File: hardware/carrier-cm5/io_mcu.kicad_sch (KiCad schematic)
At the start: 33 parts, among them J22 J-LIDAR, J30 TC2050, J31 J-ELRS, J32 U.FL 868 MHz, Q30 MMBT3904, U30 STM32C092KCT6, U31 LR1262

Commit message: cm5 carrier: lora on an rfm95w
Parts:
- removed U31: LR1262, carrier-cm5:LR1262_Elecrow, symbol carrier-cm5-extra:LR1262
- added U31: RFM95W-868S2, RF_Module:HOPERF_RFM9XW_SMD, symbol RF_Module:RFM95W-868S2
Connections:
- net LORA_BUSY is gone; now on net LORA_DIO1: U30.20 (PC6)
- net +3V3: now also U31.13 (3.3V)
- net GND: now also U31.1 (GND), U31.10 (GND), U31.8 (GND)
- net LORA_ANT: now also U31.9 (ANT)
- net LORA_DIO1: now also U31.15 (DIO1); no longer U30.22 (PA11_[PA9])
- net LORA_MISO: now also U31.2 (MISO)
- net LORA_MOSI: now also U31.3 (MOSI)
- net LORA_NRST: now also U31.6 (RESET)
- net LORA_NSS: now also U31.5 (NSS)
- net LORA_SCK: now also U31.4 (SCK)
- new net LORA_DIO0: U30.22 (PA11_[PA9]), U31.14 (DIO0)
- no-connect marks 9 -> 13

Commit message: cm5 carrier: a7670e lte sheet
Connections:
- net LTE_EN: now reaches U30.15 (PB0)
- net LTE_STATUS: now reaches U30.17 (PB2)
- no-connect marks 13 -> 11
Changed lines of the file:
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@@
 	(rectangle
 		(start 17.78 17.78)
-		(end 190.5 172.72)
+		(end 190.5 180.34)
 		(stroke
 			(width 0)
@@
 		)
 	)
-	(no_connect
-		(at 93.98 109.22)
-	)
 	(wire
 		(pts
@@
 		(at 111.76 91.44)
 	)
-	(no_connect
-		(at 111.76 93.98)
-	)
 	(wire
 		(pts
@@
 		)
 	)
+	(wire
+		(pts
+			(xy 93.98 109.22) (xy 93.98 111.76)
+		)
+		(stroke
+			(width 0)
+			(type default)
+		)
+	)
+	(label "LTE_EN"
+		(at 93.98 111.76 270)
+		(fields_autoplaced yes)
+		(effects
+			(font
+				(size 1.27 1.27)
+			)
+			(justify right bottom)
+		)
+	)
+	(wire
+		(pts
+			(xy 111.76 93.98) (xy 114.3 93.98)
+		)
+		(stroke
+			(width 0)
+			(type default)
+		)
+	)
+	(label "LTE_STATUS"
+		(at 114.3 93.98 0)
+		(fields_autoplaced yes)
+		(effects
+			(font
+				(size 1.27 1.27)
+			)
+			(justify left bottom)
+		)
+	)
+	(hierarchical_label "LTE_EN"
+		(shape bidirectional)
+		(at 125.73 170.18 180)
+		(fields_autoplaced yes)
+		(effects
+			(font
+				(size 1.27 1.27)
+			)
+			(justify right)
+		)
+	)
+	(wire
+		(pts
+			(xy 125.73 170.18) (xy 135.89 170.18)
+		)
+		(stroke
+			(width 0)
+			(type default)
+		)
+	)
+	(label "LTE_EN"
+		(at 135.89 170.18 0)
+		(fields_autoplaced yes)
+		(effects
+			(font
+				(size 1.27 1.27)
+			)
+			(justify left bottom)
+		)
+	)
+	(hierarchical_label "LTE_STATUS"
+		(shape bidirectional)
+		(at 125.73 173.99 180)
+		(fields_autoplaced yes)
+		(effects
+			(font
+				(size 1.27 1.27)
+			)
+			(justify right)
+		)
+	)
+	(wire
+		(pts
+			(xy 125.73 173.99) (xy 135.89 173.99)
+		)
+		(stroke
+			(width 0)
+			(type default)
+		)
+	)
+	(label "LTE_STATUS"
+		(at 135.89 173.99 0)
+		(fields_autoplaced yes)
+		(effects
+			(font
+				(size 1.27 1.27)
+			)
+			(justify left bottom)
+		)
+	)

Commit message: Updated schematic on CM5 carrier
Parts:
- renumbered BZ30 to BZ601, C80 to C601, C82 to C602, C81 to C603, C83 to C604, C84 to C605, C85 to C606, C86 to C607, C87 to C608, D80 to D601, D81 to D602, J30 to J601, J22 to J602, J31 to J603, J32 to J604, JP30 to JP601, JP31 to JP602, JP32 to JP603, JP33 to JP604, JP34 to JP605, Q30 to Q601, R80 to R601, R83 to R602, R84 to R603, R81 to R604, R82 to R605, R85 to R606, R86 to R607, R87 to R608, R89 to R609, R88 to R610, U30 to U601, U31 to U602
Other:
- company: AAC -> (none)
- moved on the sheet: C604, J602, J603, J604, JP605, R602, R603, R604, R605

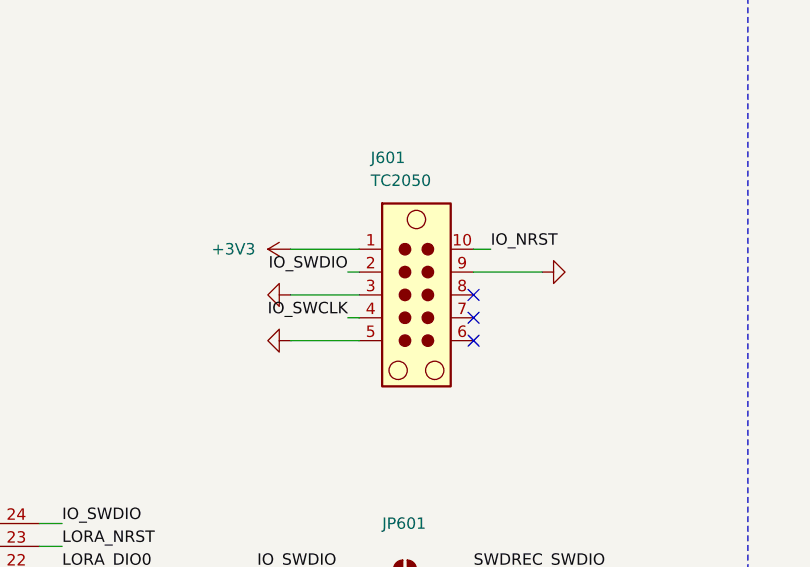
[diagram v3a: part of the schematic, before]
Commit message: carrier: xh can and sysctl connectors, io mcu wiring tidy
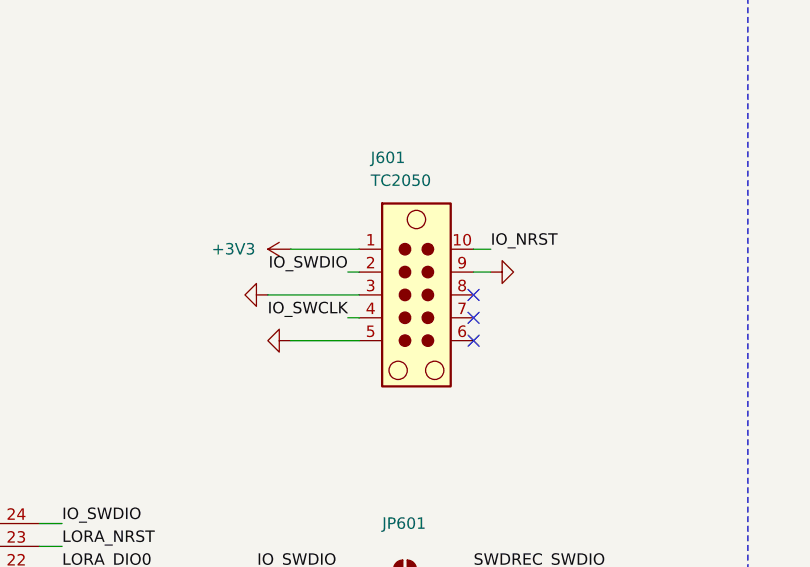
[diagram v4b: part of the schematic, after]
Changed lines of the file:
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@@
 	(wire
 		(pts
-			(xy 160.02 48.26) (xy 167.64 48.26)
+			(xy 160.02 48.26) (xy 161.925 48.26)
 		)
 		(stroke
@@
 	(wire
 		(pts
-			(xy 147.32 50.8) (xy 139.7 50.8)
+			(xy 147.32 50.8) (xy 137.16 50.8)
 		)
 		(stroke
@@
 	(symbol
 		(lib_id "power:GND")
-		(at 139.7 50.8 270)
+		(at 137.16 50.8 270)
 		(unit 1)
 		(body_style 1)
@@
 		(dnp no)
 		(property "Reference" "#PWR0610"
-			(at 139.7 57.15 0)
+			(at 137.16 57.15 0)
 			(hide yes)
 			(show_name no)
@@
 		)
 		(property "Value" "GND"
-			(at 139.7 54.61 0)
+			(at 137.16 54.61 0)
 			(hide yes)
 			(show_name no)
@@
 		)
 		(property "Footprint" ""
-			(at 139.7 50.8 0)
+			(at 137.16 50.8 0)
 			(show_name no)
 			(do_not_autoplace no)
@@
 		)
 		(property "Datasheet" ""
-			(at 139.7 50.8 0)
+			(at 137.16 50.8 0)
 			(show_name no)
 			(do_not_autoplace no)
@@
 		)
 		(property "Description" ""
-			(at 139.7 50.8 0)
+			(at 137.16 50.8 0)
 			(show_name no)
 			(do_not_autoplace no)
@@
 	(symbol
 		(lib_id "power:GND")
-		(at 167.64 48.26 90)
+		(at 161.925 48.26 90)
 		(unit 1)
 		(body_style 1)
@@
 		(dnp no)
 		(property "Reference" "#PWR0612"
-			(at 167.64 54.61 0)
+			(at 161.925 54.61 0)
 			(hide yes)
 			(show_name no)
@@
 		)
 		(property "Value" "GND"
-			(at 167.64 52.07 0)
+			(at 161.925 52.07 0)
 			(hide yes)
 			(show_name no)
@@
 		)
 		(property "Footprint" ""
-			(at 167.64 48.26 0)
+			(at 161.925 48.26 0)
 			(show_name no)
 			(do_not_autoplace no)
@@
 		)
 		(property "Datasheet" ""
-			(at 167.64 48.26 0)
+			(at 161.925 48.26 0)
 			(show_name no)
 			(do_not_autoplace no)
@@
 		)
 		(property "Description" ""
-			(at 167.64 48.26 0)
+			(at 161.925 48.26 0)
 			(show_name no)
 			(do_not_autoplace no)

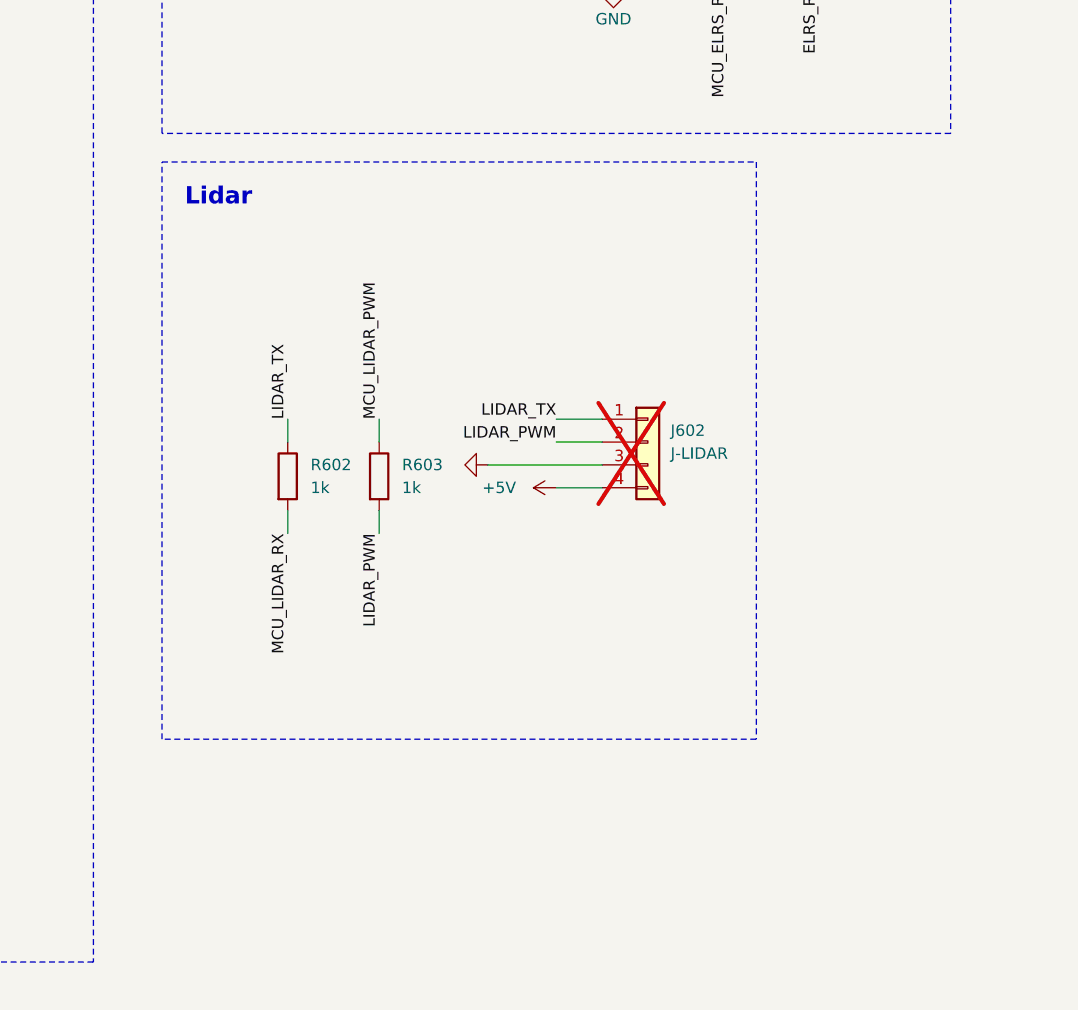
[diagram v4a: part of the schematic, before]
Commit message: add lidar motor fet and xh connectors on carrier
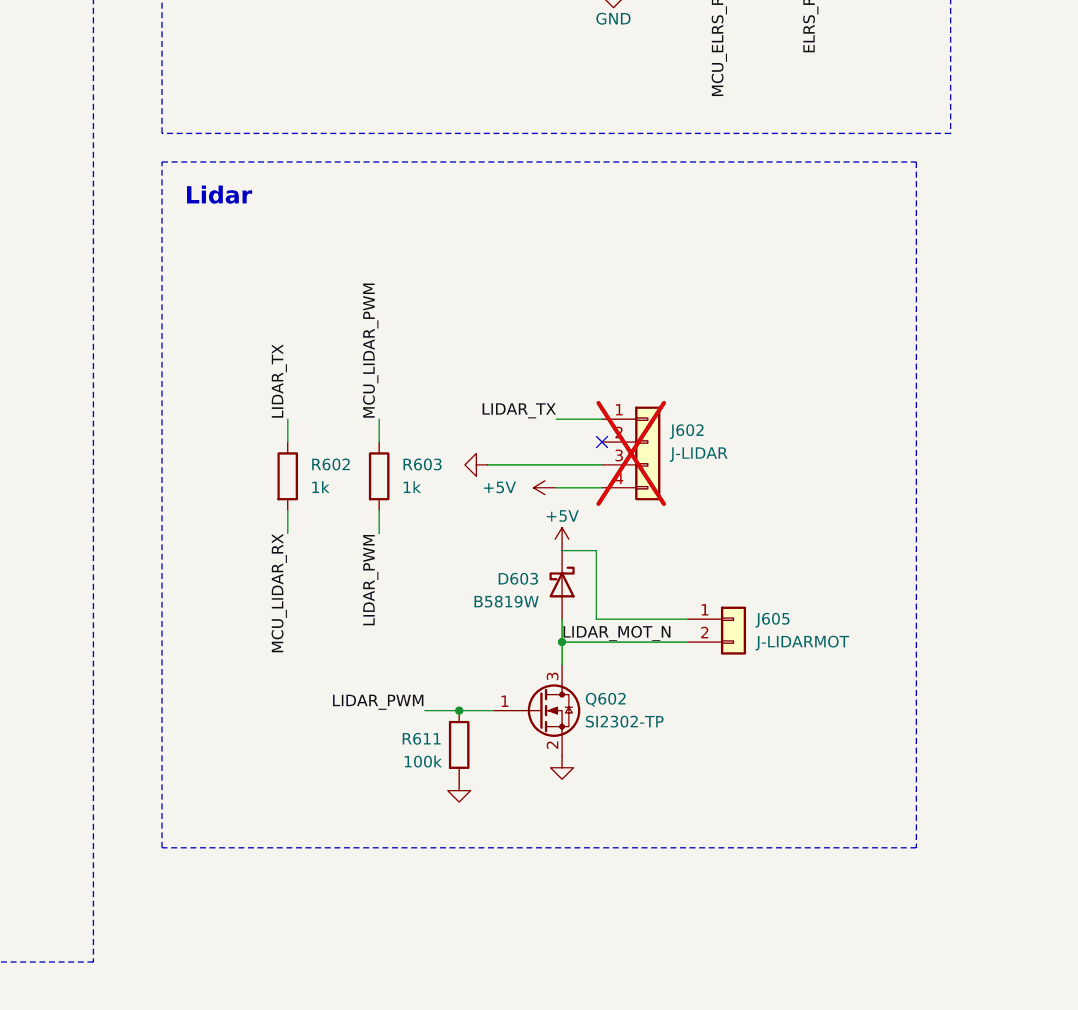
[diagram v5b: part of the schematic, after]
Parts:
- added D603: B5819W, Diode_SMD:D_SOD-123, symbol Device:D_Schottky
- added J605: J-LIDARMOT, Connector_JST:JST_XH_B2B-XH-A_1x02_P2.50mm_Vertical, symbol Connector_Generic:Conn_01x02
- added Q602: SI2302-TP, Package_TO_SOT_SMD:SOT-23, symbol Transistor_FET:Q_NMOS_GSD
- added R611: 100k, Resistor_SMD:R_0402_1005Metric, symbol Device:R
- J602: footprint Connector_JST:JST_GH_SM04B-GHS-TB_1x04-1MP_P1.25mm_Horizontal -> Connector_JST:JST_XH_B4B-XH-A_1x04_P2.50mm_Vertical
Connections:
- net +5V: now also D603.1 (K), J605.1 (Pin_1)
- net GND: now also Q602.2 (S), R611.2
- net LIDAR_PWM: now also Q602.1 (G), R611.1; no longer J602.2 (Pin_2)
- new net LIDAR_MOT_N: D603.2 (A), J605.2 (Pin_2), Q602.3 (D)
- no-connect marks 11 -> 12
